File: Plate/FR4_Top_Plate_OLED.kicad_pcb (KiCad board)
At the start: 2 copper layers, 139.1 x 107.7 mm, 34 parts, among them SW1 SW_PUSH, SW10 SW_PUSH, SW11 SW_PUSH, SW12 SW_PUSH, SW13 SW_PUSH, SW14 SW_PUSH, SW15 SW_PUSH, SW16 SW_PUSH, SW17 SW_PUSH, SW18 SW_PUSH, SW19 SW_PUSH, SW2 SW_PUSH, SW20 SW_PUSH, SW21 SW_PUSH, SW22 SW_PUSH, SW23 SW_PUSH, SW24 SW_PUSH, SW25 SW_PUSH, SW26 SW_PUSH, SW27 SW_PUSH, SW28 SW_PUSH, SW29 SW_PUSH, SW3 SW_PUSH, SW4 SW_PUSH, SW5 SW_PUSH, SW6 SW_PUSH, SW7 SW_PUSH, SW8 SW_PUSH, SW9 SW_PUSH

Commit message: Updated plates
Plates now have no copper layer, both preparing for wireless, and to avoid scratches/shorting, if OLED etc. is not soldered with flat pads.
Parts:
- SW1, SW10, SW11, SW12, SW13, SW14, SW15, SW16, SW17, SW18, SW19, SW2, SW20, SW21, SW22, SW23, SW24, SW25, SW26, SW27, SW28, SW29, SW3, SW4, SW5, SW6, SW7, SW8, SW9: footprint Keyboard Library:Cherry_MX_Plate_Hole_Placeholder -> Keyboard_Plate:SW_MX_Plate_Placeholder_nodrill_NOBORDER_13,9
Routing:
- removed copper zone on B.Cu, net (none)
- removed copper zone on F.Cu, net (none)
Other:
- net class Default removed
- net class GND removed
- net class VCC removed
- board text removed: "Lotus58 Glow"

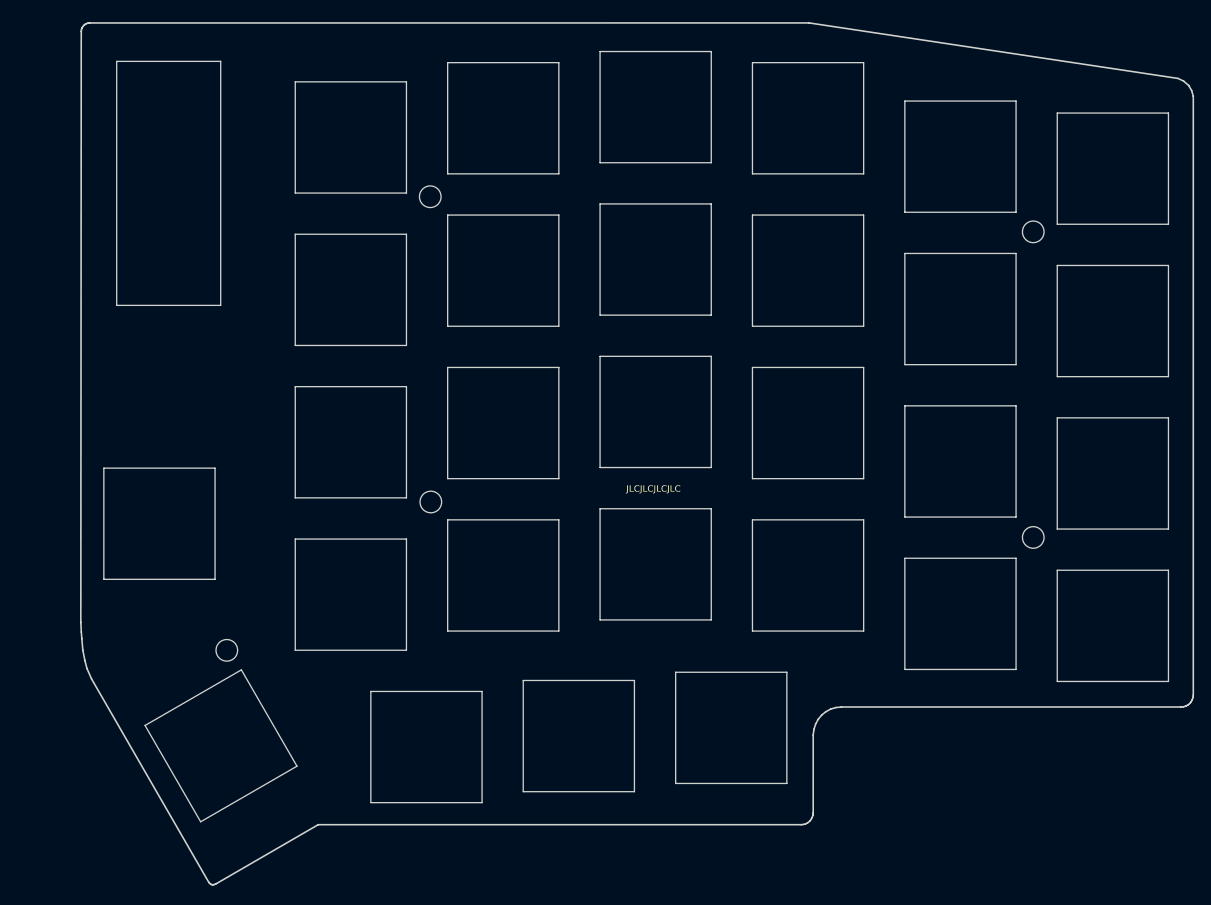
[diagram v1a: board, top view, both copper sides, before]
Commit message: Revert "Merge pull request #53 from TweetyDaBird/release"
This reverts commit d5395b9879702c31b6de7b44cd45c4487da02165, reversing
changes made to 721366541e1b3daa08e8a27e832954bcb38f5212.

# Conflicts:
#	.gitignore
#	Lotus 58 Classic/v1.26/Lotus58_Glow_126.kicad_pcb
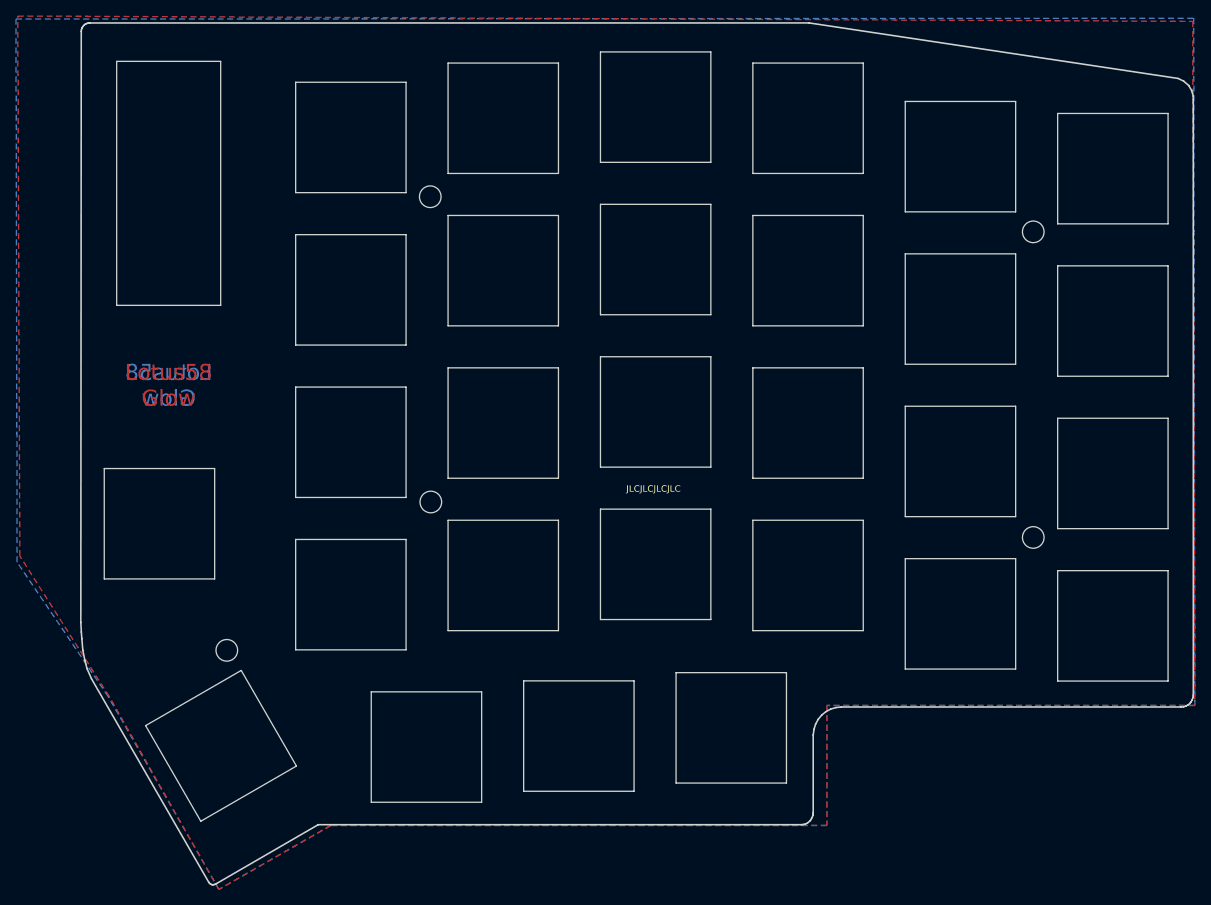
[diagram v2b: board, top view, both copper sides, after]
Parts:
- SW1, SW10, SW11, SW12, SW13, SW14, SW15, SW16, SW17, SW18, SW19, SW2, SW20, SW21, SW22, SW23, SW24, SW25, SW26, SW27, SW28, SW29, SW3, SW4, SW5, SW6, SW7, SW8, SW9: footprint Keyboard_Plate:SW_MX_Plate_Placeholder_nodrill_NOBORDER_13,9 -> Keyboard Library:Cherry_MX_Plate_Hole_Placeholder
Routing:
- added copper zone on B.Cu, net (none)
- added copper zone on F.Cu, net (none)
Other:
- net class Default added: clearance 0.2, trace_width 0.25, via_dia 0.6096, via_drill 0.3048
- net class GND added: clearance 0.2, trace_width 0.5, via_dia 0.8128, via_drill 0.3048
- net class VCC added: clearance 0.2, trace_width 0.5, via_dia 0.8128, via_drill 0.3048
- board text added: "Lotus58 Glow"
